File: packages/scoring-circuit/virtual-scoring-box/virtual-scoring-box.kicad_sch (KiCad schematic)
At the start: 0 parts

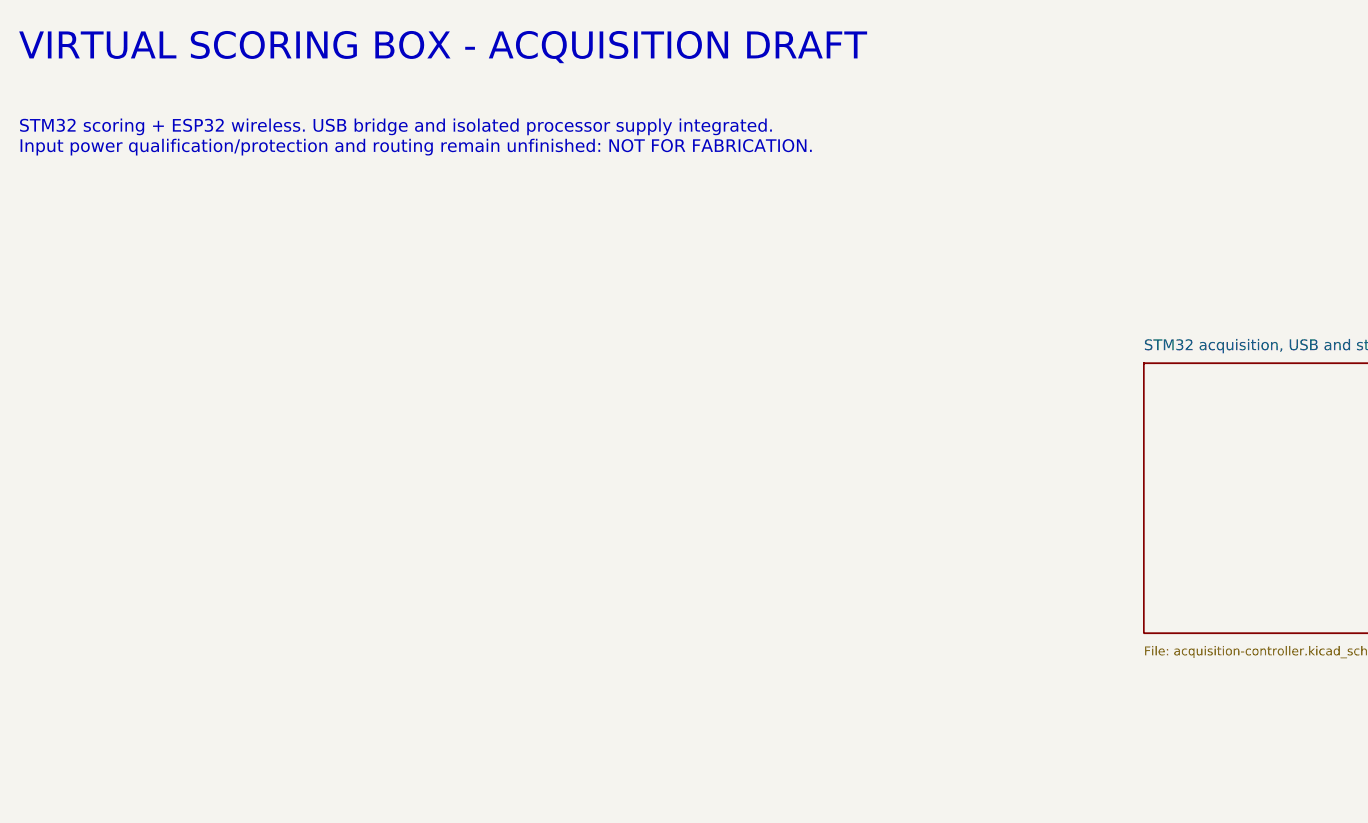
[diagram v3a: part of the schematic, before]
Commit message: feat(scoring-circuit): integrate virtual-box USB-C source control
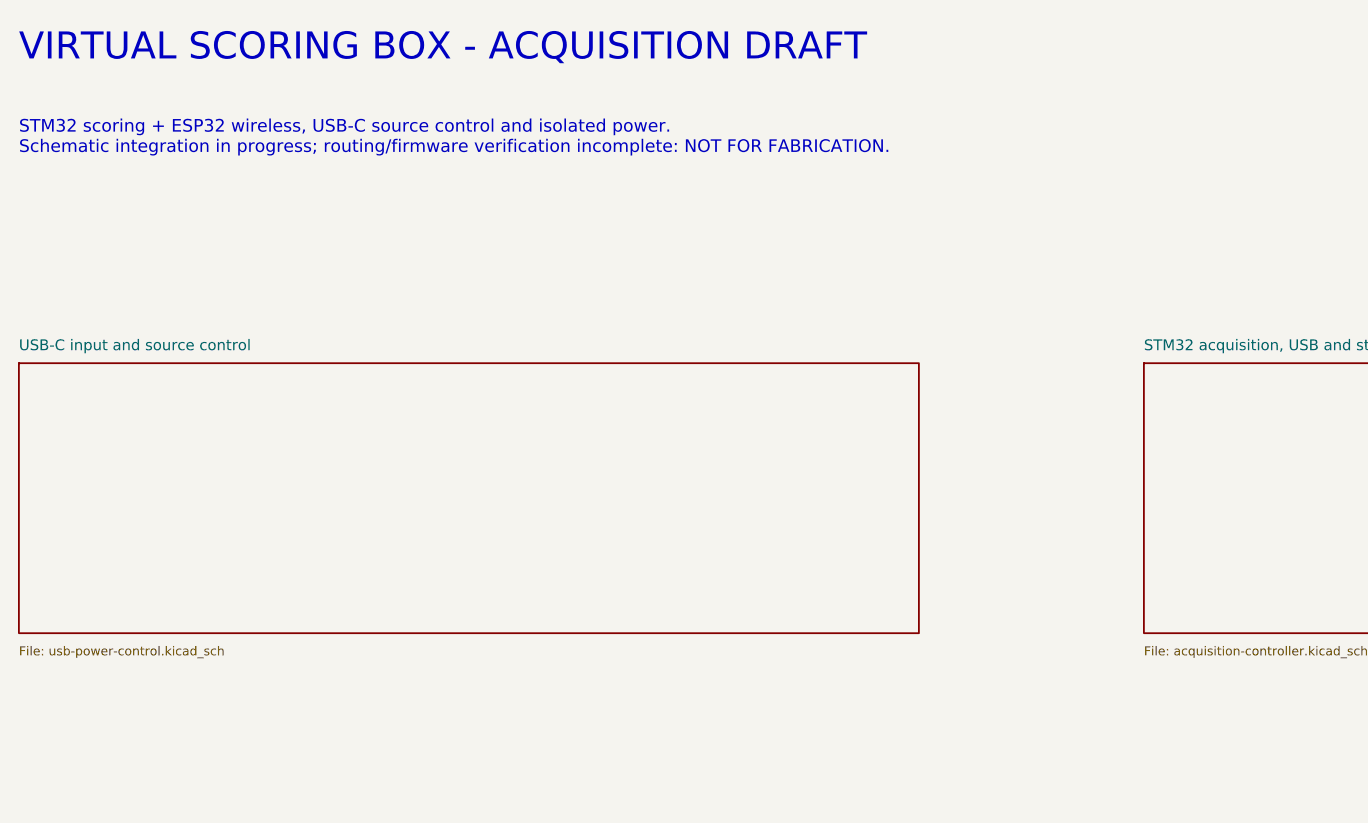
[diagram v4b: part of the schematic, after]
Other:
- added sheet USB-C input and source control (usb-power-control.kicad_sch)
- note added: "STM32 scoring + ESP32 wireless, USB-C source control and isolated power. Schematic integration in progress; routing/firmware verification incomplete: NOT FOR FABRICATION."
- note removed: "STM32 scoring + ESP32 wireless. USB bridge and isolated processor supply integrated. Input power qualification/protection and routing remain unfinished: NOT FOR FABRICATION."
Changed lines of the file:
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@@
 (title_block (title "Virtual scoring box") (rev "Engineering draft") (comment 1 "Separate design - original prototype preserved"))
 (text "VIRTUAL SCORING BOX - ACQUISITION DRAFT" (at 30 20 0) (effects (font (size 3 3)) (justify left)))
-(text "STM32 scoring + ESP32 wireless. USB bridge and isolated processor supply integrated.\nInput power qualification/protection and routing remain unfinished: NOT FOR FABRICATION." (at 30 30 0) (effects (font (size 1.4 1.4)) (justify left)))
+(text "STM32 scoring + ESP32 wireless, USB-C source control and isolated power.\nSchematic integration in progress; routing/firmware verification incomplete: NOT FOR FABRICATION." (at 30 30 0) (effects (font (size 1.4 1.4)) (justify left)))
 (sheet (at 155 55) (size 100 30) (stroke (width 0.2) (type default)) (fill (color 0 0 0 0)) (property "Sheetname" "STM32 acquisition, USB and standalone scoring" (at 155 53 0) (effects (font (size 1.2 1.2)) (justify left))) (property "Sheetfile" "acquisition-controller.kicad_sch" (at 155 87 0) (effects (font (size 1 1)) (justify left))) (instances (project "virtual-scoring-box" (path "/20cc8167-128c-446a-a106-f942323e143f" (page "3")))))
 (sheet (at 280 55) (size 100 30) (stroke (width 0.2) (type default)) (fill (color 0 0 0 0)) (property "Sheetname" "Left weapon acquisition" (at 280 53 0) (effects (font (size 1.2 1.2)) (justify left))) (property "Sheetfile" "left-weapon-inputs.kicad_sch" (at 280 87 0) (effects (font (size 1 1)) (justify left))) (instances (project "virtual-scoring-box" (path "/20cc8167-128c-446a-a106-f942323e143f" (page "4")))))
@@
 (sheet (at 280 110) (size 100 30) (stroke (width 0.2) (type default)) (fill (color 0 0 0 0)) (property "Sheetname" "IR remote receiver" (at 280 108 0) (effects (font (size 1.2 1.2)) (justify left))) (property "Sheetfile" "ir-receiver.kicad_sch" (at 280 142 0) (effects (font (size 1 1)) (justify left))) (instances (project "virtual-scoring-box" (path "/20cc8167-128c-446a-a106-f942323e143f" (page "7")))))
 (sheet (at 280 165) (size 100 30) (stroke (width .2) (type default)) (fill (color 0 0 0 0)) (property "Sheetname" "Isolated processor supply" (at 280 163 0) (effects (font (size 1.2 1.2)) (justify left))) (property "Sheetfile" "isolated-power.kicad_sch" (at 280 197 0) (effects (font (size 1 1)) (justify left))) (instances (project "virtual-scoring-box" (path "/20cc8167-128c-446a-a106-f942323e143f" (page "10")))))
+(sheet (at 30 55) (size 100 30) (stroke (width .2) (type default)) (fill (color 0 0 0 0)) (property "Sheetname" "USB-C input and source control" (at 30 53 0) (effects (font (size 1.2 1.2)) (justify left))) (property "Sheetfile" "usb-power-control.kicad_sch" (at 30 87 0) (effects (font (size 1 1)) (justify left))) (instances (project "virtual-scoring-box" (path "/20cc8167-128c-446a-a106-f942323e143f" (page "2")))))
 )
